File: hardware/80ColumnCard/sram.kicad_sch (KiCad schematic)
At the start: 7 parts, among them U10 6116, U10N28 '32 - '256, U10N32 '512, U10W24 6116, U10W28 '32 - '256, U10W32 '512, X21 A11/WE

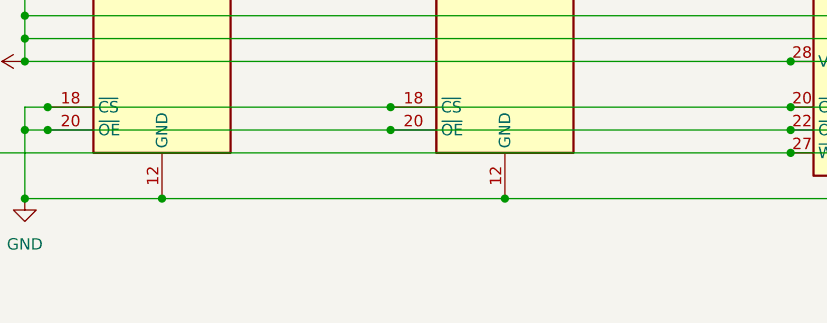
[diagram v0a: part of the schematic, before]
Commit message: clean up, add jumpers for fw/char selection
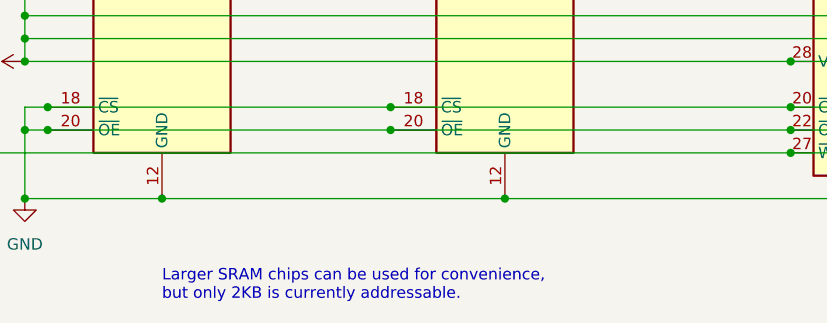
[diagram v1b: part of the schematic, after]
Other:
- note added: "Larger SRAM chips can be used for convenience, but only 2KB is currently addressable."
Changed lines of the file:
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@@
     (stroke (width 0) (type default) (color 0 0 0 0))
+  )
+  (text "Larger SRAM chips can be used for convenience, \nbut only 2KB is currently addressable."
+    (at 50.8 123.19 0)
+    (effects (font (size 1.27 1.27)) (justify left bottom))
   )
   (hierarchical_label "RAMA1" (shape input) (at 25.4 76.2 180)

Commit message: fiddling
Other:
- moved on the sheet: U10N28, U10N32, U10W24, U10W28, U10W32

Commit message: revert fiddling
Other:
- note removed: "Larger SRAM chips can be used for convenience, but only 2KB is currently addressable."
- moved on the sheet: U10N28, U10N32, U10W24, U10W28, U10W32
